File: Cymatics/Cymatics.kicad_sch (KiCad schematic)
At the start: 68 parts, among them IC1 LMV358IDR, IC2 MAX7403CSA+, IC3 LMV358IDR, IC4 LMV358IDR, IC5 MAX7403CSA+, J1 Screw_Terminal_01x03, J10 Screw_Terminal_01x04, J11 Screw_Terminal_01x05, J12 Screw_Terminal_01x02, J13 Screw_Terminal_01x02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

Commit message: resolved all DRC errors
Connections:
- net EXT_CS: now also J6.10 (Pin_10); no longer J6.15 (Pin_15)
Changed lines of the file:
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@@
-		)
-	)
-	(global_label "EXT_CS"
-		(shape output)
-		(at 147.32 226.06 180)
-		(fields_autoplaced yes)
-		(effects
-			(font
-				(size 1.27 1.27)
-			)
-			(justify right)
-		)
-		(property "Intersheetrefs" "${INTERSHEET_REFS}"
-			(at 137.5616 226.06 0)
-			(effects
-				(font
-					(size 1.27 1.27)
-				)
-				(justify right)
-				(hide yes)
-			)
 		)
 	)
@@
 				(hide yes)
 			)
+		)
+	)
+	(global_label "EXT_CS"
+		(shape output)
+		(at 147.32 213.36 180)
+		(fields_autoplaced yes)
+		(effects
+			(font
+				(size 1.27 1.27)
+			)
+			(justify right)
+		)
+		(property "Intersheetrefs" "${INTERSHEET_REFS}"
+			(at 137.5616 213.36 0)
+			(effects
+				(font
+					(size 1.27 1.27)
+				)
+				(justify right)
+				(hide yes)
+			)

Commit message: added testpoints
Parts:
- added TP1, TP2, TP3: TestPoint_2Pole, TestPoint:TestPoint_2Pads_Pitch2.54mm_Drill0.8mm, symbol Connector:TestPoint_2Pole
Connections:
- net GND: now also TP1.2, TP2.2, TP3.2
- net at IC1.7 (2OUT), IC2.2 (IN), R1.1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: now also TP1.1
- net at IC4.7 (2OUT), IC5.2 (IN), R2.2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: now also TP2.1
- net at R1.2, R2.1, U2.2 (IN): now also TP3.1
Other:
- moved on the sheet: C1, C10, C11, C12, C13, C14, C15, C16, C18, C19, C2, C3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

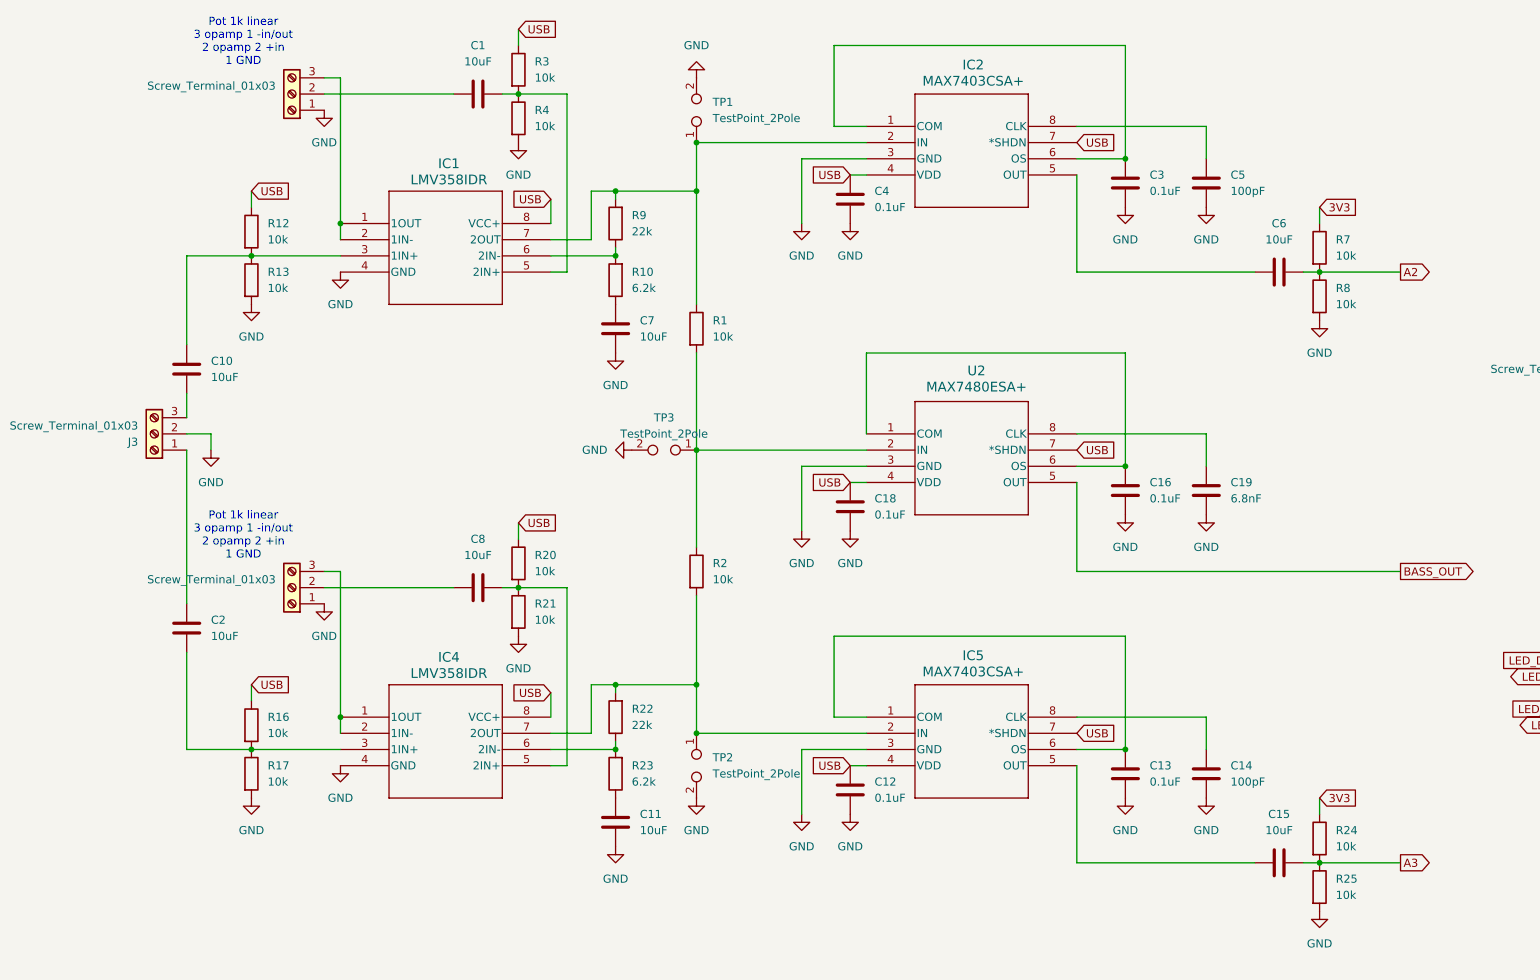
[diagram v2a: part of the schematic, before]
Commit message: testpoints update and terminal block labels
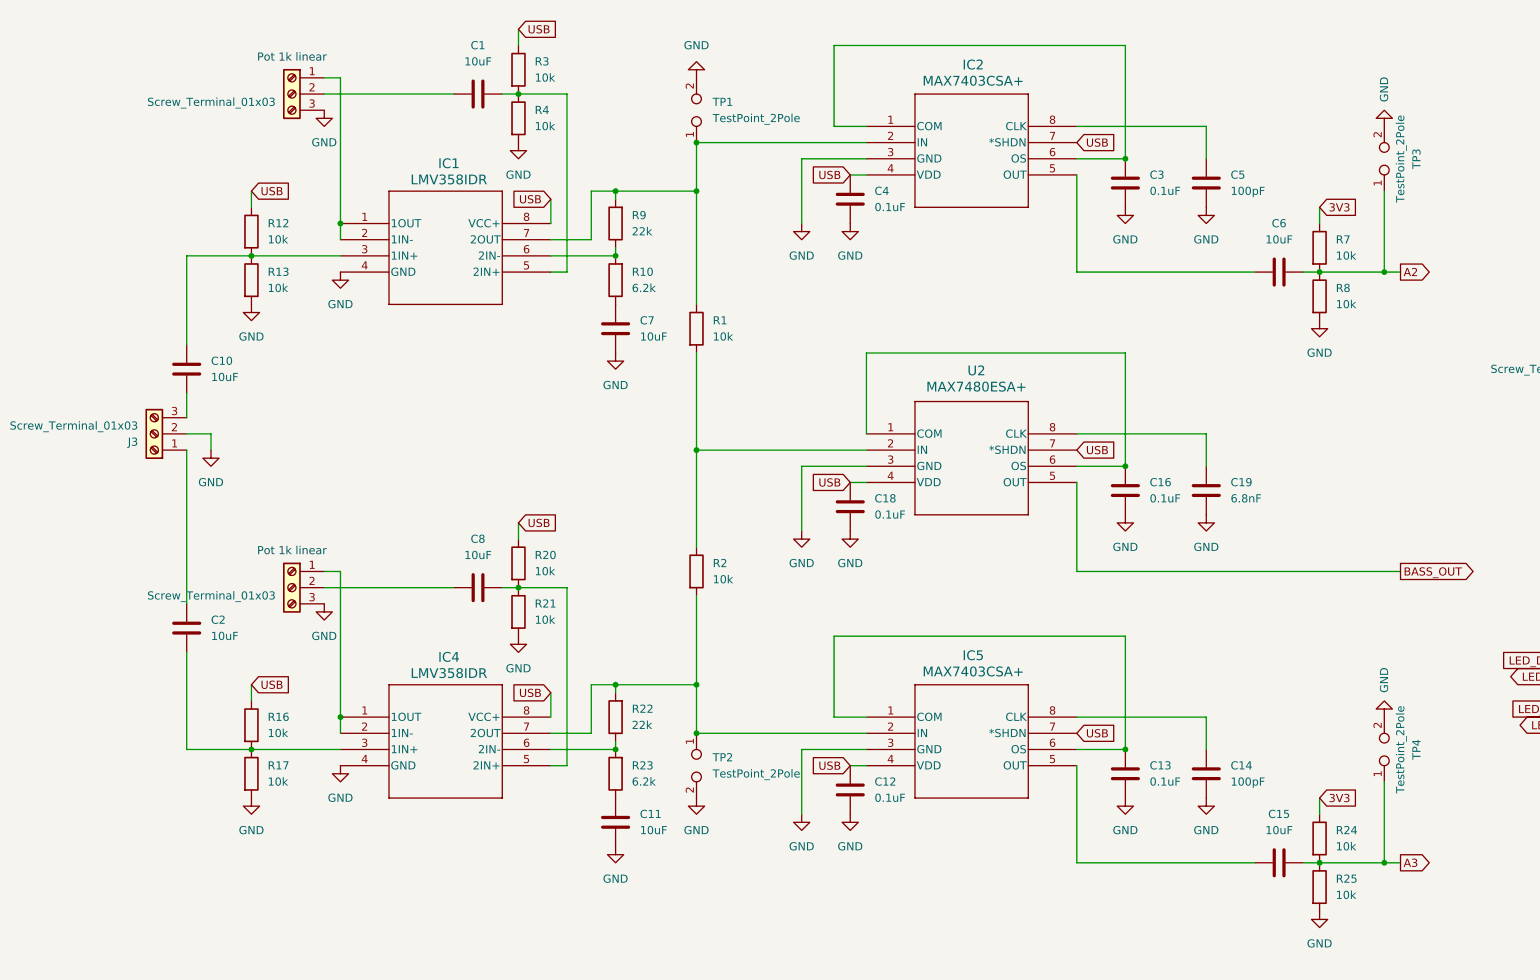
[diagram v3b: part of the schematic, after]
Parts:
- added TP4: TestPoint_2Pole, TestPoint:TestPoint_2Pads_Pitch2.54mm_Drill0.8mm, symbol Connector:TestPoint_2Pole
- C1, C10, C11, C15, C2, C6, C7, C8, J1, J16, J3, J4: In Stock 01-31-25 (none) -> 12
- C12, C13, C16, C18, C3, C4, C9: In Stock 01-31-25 (none) -> 10
- C14, C5, IC1, IC3, IC4, R10, R11, R14, R22, R23, R5, R6, R9: In Stock 01-31-25 (none) -> 8
- C17, IC2, IC5, J11, J6, J7, SD1, U1: In Stock 01-31-25 (none) -> 3
- C19, J18, TP1, TP2, TP3, U2: In Stock 01-31-25 (none) -> 0
- J10, J8: In Stock 01-31-25 (none) -> 4
- J12, J13, J15, J17, J2, J5, J9: In Stock 01-31-25 (none) -> 9
- R1, R12, R13, R16, R17, R18, R19, R2, R20, R21, R24, R25, R3, R4, R7, R8: In Stock 01-31-25 (none) -> 30
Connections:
- net A2: now also TP3.1
- net A3: now also TP4.1
- net GND: now also J16.3 (Pin_3), J4.3 (Pin_3), TP4.2; no longer J16.1 (Pin_1), J4.1 (Pin_1)
- net at IC1.1 (1OUT), IC1.2 (1IN-): now also J4.1 (Pin_1); no longer J4.3 (Pin_3)
- net at R1.2, R2.1, U2.2 (IN): no longer TP3.1
- net at IC4.1 (1OUT), IC4.2 (1IN-): now also J16.1 (Pin_1); no longer J16.3 (Pin_3)
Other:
- note added: "Pot 1k linear"
- note removed: "Pot 1k linear 3 opamp 1 -in/out 2 opamp 2 +in 1 GND"

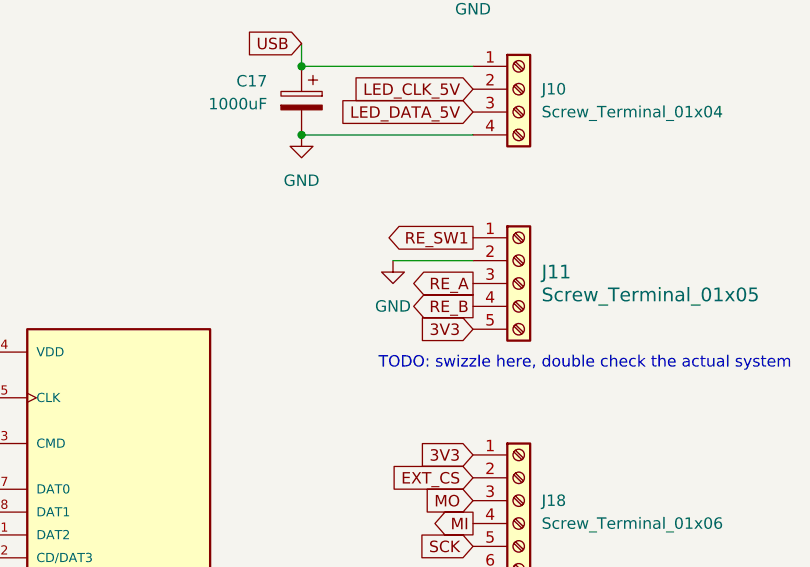
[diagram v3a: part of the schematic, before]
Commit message: swizzled rotary encoder block
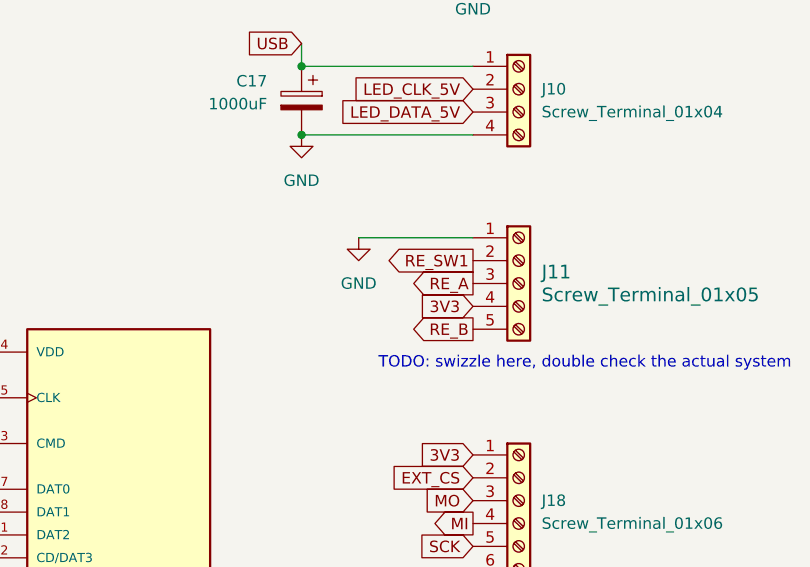
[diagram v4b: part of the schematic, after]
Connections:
- net 3V3: now also J11.4 (Pin_4); no longer J11.5 (Pin_5)
- net GND: now also J11.1 (Pin_1); no longer J11.2 (Pin_2)
- net RE_B: now also J11.5 (Pin_5); no longer J11.4 (Pin_4)
- net RE_SW1: now also J11.2 (Pin_2); no longer J11.1 (Pin_1)
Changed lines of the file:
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@@
 	(wire
 		(pts
-			(xy 358.14 177.8) (xy 367.03 177.8)
-		)
-		(stroke
-			(width 0)
-			(type default)
-		)
-	)
-	(wire
-		(pts
 			(xy 267.97 134.62) (xy 267.97 142.24)
 		)
@@
 	(wire
 		(pts
+			(xy 354.33 175.26) (xy 367.03 175.26)
+		)
+		(stroke
+			(width 0)
+			(type default)
+		)
+	)
+	(wire
+		(pts
 			(xy 321.31 76.2) (xy 321.31 83.82)
 		)
@@
 		)
 	)
-	(global_label "RE_B"
-		(shape output)
-		(at 367.03 182.88 180)
-		(fields_autoplaced yes)
-		(effects
-			(font
-				(size 1.27 1.27)
-			)
-			(justify right)
-		)
-		(property "Intersheetrefs" "${INTERSHEET_REFS}"
-			(at 359.3882 182.88 0)
-			(effects
-				(font
-					(size 1.27 1.27)
-				)
-				(justify right)
-				(hide yes)
-			)
-		)
-	)
 	(global_label "3V3"
 		(shape input)
@@
 		)
 	)
-	(global_label "3V3"
-		(shape input)
-		(at 367.03 185.42 180)
-		(fields_autoplaced yes)
-		(effects
-			(font
-				(size 1.27 1.27)
-			)
-			(justify right)
-		)
-		(property "Intersheetrefs" "${INTERSHEET_REFS}"
-			(at 360.5372 185.42 0)
-			(effects
-				(font
-					(size 1.27 1.27)
-				)
-				(justify right)
-				(hide yes)
-			)
-		)
-	)
 	(global_label "LED_CLK_3V3"
 		(shape input)
@@
 		)
 	)
-	(global_label "RE_SW1"
-		(shape output)
-		(at 367.03 175.26 180)
-		(fields_autoplaced yes)
-		(effects
-			(font
-				(size 1.27 1.27)
-			)
-			(justify right)
-		)
-		(property "Intersheetrefs" "${INTERSHEET_REFS}"
-			(at 356.7878 175.26 0)
-			(effects
-				(font
-					(size 1.27 1.27)
-				)
-				(justify right)
-				(hide yes)
-			)
-		)
-	)
 	(global_label "3V3"
 		(shape input)
@@
 		)
 	)
+	(global_label "RE_SW1"
+		(shape output)
+		(at 367.03 177.8 180)
+		(fields_autoplaced yes)
+		(effects
+			(font
+				(size 1.27 1.27)
+			)
+			(justify right)
+		)
+		(property "Intersheetrefs" "${INTERSHEET_REFS}"
+			(at 356.7878 177.8 0)
+			(effects
+				(font
+					(size 1.27 1.27)
+				)
+				(justify right)
+				(hide yes)
+			)
+		)
+	)
+	(global_label "RE_B"
+		(shape output)
+		(at 367.03 185.42 180)
+		(fields_autoplaced yes)
+		(effects
+			(font
+				(size 1.27 1.27)
+			)
+			(justify right)
+		)
+		(property "Intersheetrefs" "${INTERSHEET_REFS}"
+			(at 359.3882 185.42 0)
+			(effects
+				(font
+					(size 1.27 1.27)
+				)
+				(justify right)
+				(hide yes)
+			)
+		)
+	)
 	(global_label "USB"
 		(shape input)
@@
 		)
 	)
+	(global_label "3V3"
+		(shape input)
+		(at 367.03 182.88 180)
+		(fields_autoplaced yes)
+		(effects
+			(font
+				(size 1.27 1.27)
+			)
+			(justify right)
+		)
+		(property "Intersheetrefs" "${INTERSHEET_REFS}"
+			(at 360.5372 182.88 0)
+			(effects
+				(font
+					(size 1.27 1.27)
+				)
+				(justify right)
+				(hide yes)
+			)
+		)
+	)
 	(symbol
 		(lib_id "Device:R")
@@
 	(symbol
 		(lib_id "power:GND")
-		(at 358.14 177.8 0)
-		(unit 1)
-		(exclude_from_sim no)
-		(in_bom yes)
-		(on_board yes)
-		(dnp no)
-		(fields_autoplaced yes)
-		(property "Reference" "#PWR021"
-			(at 358.14 184.15 0)
-			(effects
-				(font
-					(size 1.27 1.27)
-				)
-				(hide yes)
-			)
-		)
-		(property "Value" "GND"
-			(at 358.14 182.88 0)
-			(effects
-				(font
-					(size 1.27 1.27)
-				)
-			)
-		)
-		(property "Footprint" ""
-			(at 358.14 177.8 0)
-			(effects
-				(font
-					(size 1.27 1.27)
-				)
-				(hide yes)
-			)
-		)
-		(property "Datasheet" ""
-			(at 358.14 177.8 0)
-			(effects
-				(font
-					(size 1.27 1.27)
-				)
-				(hide yes)
-			)
-		)
-		(property "Description" "Power symbol creates a global label with name \"GND\" , ground"
-			(at 358.14 177.8 0)
-			(effects
-				(font
-					(size 1.27 1.27)
-				)
-				(hide yes)
-			)
-		)
-		(pin "1"
-		)
-		(instances
-			(project "AudioLux"
-				(path "/c40baf00-5d70-4382-8f24-d28e6ebf545d"
-					(reference "#PWR021")
-					(unit 1)
-				)
-			)
-		)
-	)
-	(symbol
-		(lib_id "power:GND")
 		(at 139.7 153.67 0)
 		(unit 1)
@@
 					(unit 1)
 				)
+			)
+		)
+	)
+	(symbol
+		(lib_id "power:GND")
+		(at 354.33 175.26 0)
+		(unit 1)
+		(exclude_from_sim no)
+		(in_bom yes)
+		(on_board yes)
+		(dnp no)
+		(fields_autoplaced yes)
+		(property "Reference" "#PWR021"
+			(at 354.33 181.61 0)
+			(effects
+				(font
+					(size 1.27 1.27)
+				)
+				(hide yes)
+			)
+		)
+		(property "Value" "GND"
+			(at 354.33 180.34 0)
+			(effects
+				(font
+					(size 1.27 1.27)
+				)
+			)
+		)
+		(property "Footprint" ""
+			(at 354.33 175.26 0)
+			(effects
+				(font
+					(size 1.27 1.27)
+				)
+				(hide yes)
+			)
+		)
+		(property "Datasheet" ""
+			(at 354.33 175.26 0)
+			(effects
+				(font
+					(size 1.27 1.27)
+				)
+				(hide yes)
+			)
+		)
+		(property "Description" "Power symbol creates a global label with name \"GND\" , ground"
+			(at 354.33 175.26 0)
+			(effects
+				(font
+					(size 1.27 1.27)
+				)
+				(hide yes)
+			)
+		)
+		(pin "1"
+		)
+		(instances
+			(project "Cymatics"
+				(path "/c40baf00-5d70-4382-8f24-d28e6ebf545d"
+					(reference "#PWR021")
+					(unit 1)
+				)

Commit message: new testpoint RCU-0C
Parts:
- removed TP1, TP2, TP3, TP4: TestPoint_2Pole, TestPoint:TestPoint_2Pads_Pitch2.54mm_Drill0.8mm, symbol Connector:TestPoint_2Pole
- added J14, J19, J20, J21, J22, J23, J24: RCU-0C, CONN1_RCU-0C_TEC, symbol RCU-0C:RCU-0C
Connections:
- net A2: now also J22.1
- net A3: now also J23.1
- net GND: now also J19.1, J21.1, J24.1
- net at IC1.7 (2OUT), IC2.2 (IN), R1.1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: now also J14.1
- net at IC4.7 (2OUT), IC5.2 (IN), R2.2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: now also J20.1

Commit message: changes and Gerber Drill generate for order
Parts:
- C1, C10, C11, C15, C2, C6, C7, C8: In Stock 02-01-25 (none) -> 8; To Order 02-01-25 (none) -> 10
- C12, C13, C16, C18, C3, C4, C9: In Stock 02-01-25 (none) -> 5; To Order 02-01-25 (none) -> 10
- C14, C5, R10, R11, R14, R22, R23, R5, R6, R9: In Stock 02-01-25 (none) -> 7; To Order 02-01-25 (none) -> 0
- C17, IC2, IC5, J11, J6, J7, SD1, U1: In Stock 02-01-25 (none) -> 2; To Order 02-01-25 (none) -> 0
- C19: In Stock 02-01-25 (none) -> 0; To Order 02-01-25 (none) -> 10
- IC1, IC3, IC4, J12, J13, J15, J17, J2, J5, J9: In Stock 02-01-25 (none) -> 6; To Order 02-01-25 (none) -> 0
- J1, J16, J3, J4: In Stock 02-01-25 (none) -> 10; To Order 02-01-25 (none) -> 0
- J10, J8: In Stock 02-01-25 (none) -> 3; To Order 02-01-25 (none) -> 0
- J14, J19, J20, J21, J22, J23, J24: In Stock 01-31-25 (none) -> 0; In Stock 02-01-25 (none) -> 0; To Order 02-01-25 (none) -> 10
- J18: In Stock 02-01-25 (none) -> 0; To Order 02-01-25 (none) -> 0
- R1, R12, R13, R16, R17, R18, R19, R2, R20, R21, R24, R25, R3, R4, R7, R8: In Stock 02-01-25 (none) -> 20; To Order 02-01-25 (none) -> 0
- U2: In Stock 02-01-25 (none) -> 0; To Order 02-01-25 (none) -> 1

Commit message: changed positioning of blocks for diagrams
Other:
- note removed: "TODO: just use 3V3?"
- note removed: "TODO: swizzle here, double check the actual system"
- moved on the sheet: C1, C10, C11, C12, C13, C14, C15, C16, C17, C18, C19, C2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

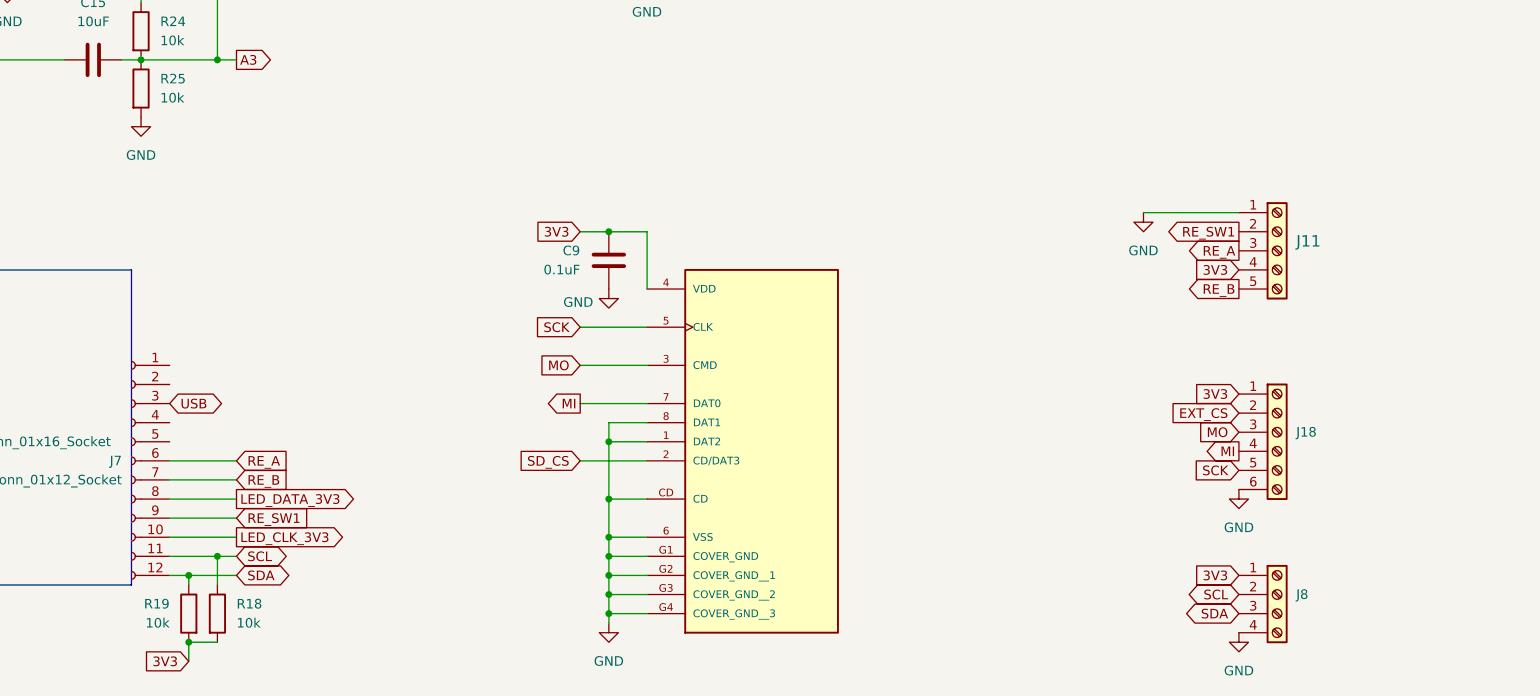
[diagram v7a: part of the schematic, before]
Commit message: pull up resistors for SPI and I2C
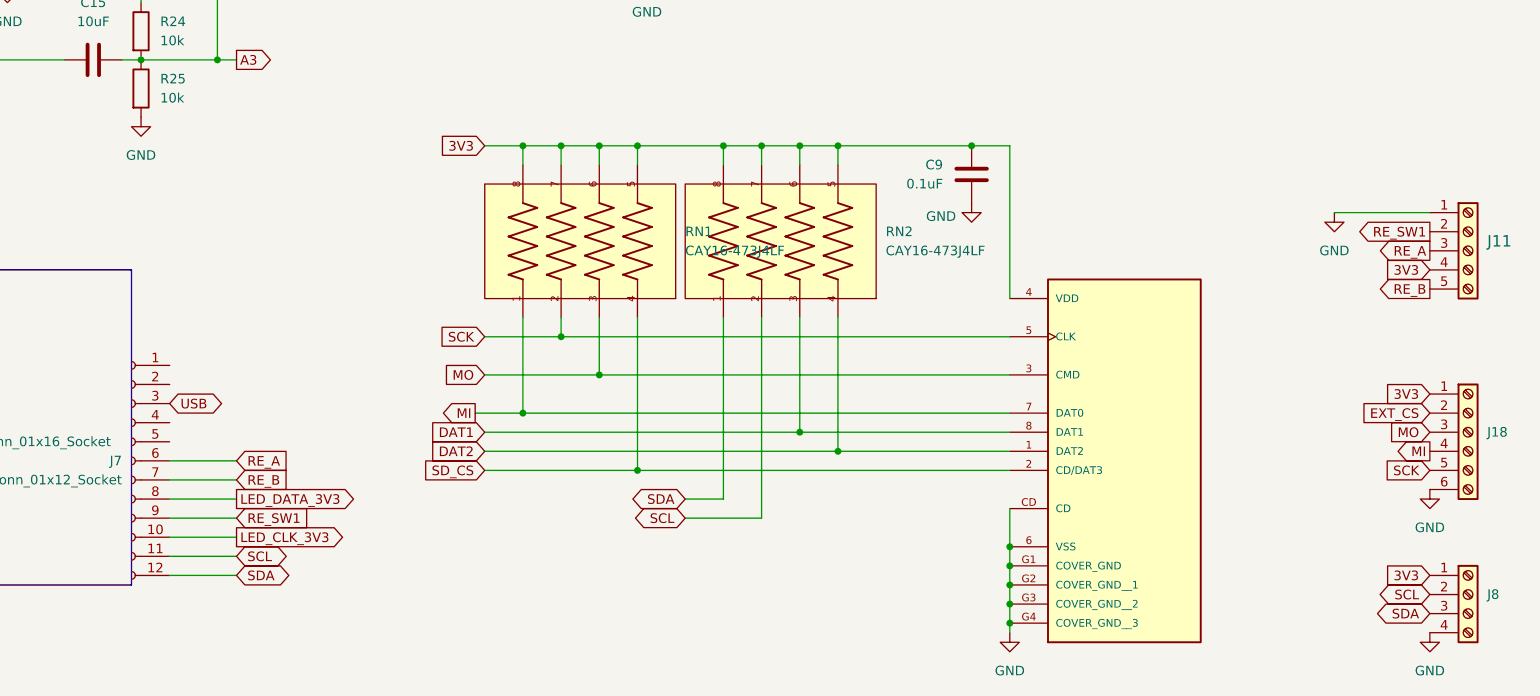
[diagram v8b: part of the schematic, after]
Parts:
- removed R18, R19: 10k, Resistor_SMD:R_1206_3216Metric, symbol Device:R
- added RN1, RN2: CAY16-473J4LF, CAY16:RESCAF80P320X160X60-8N, symbol CAY16:CAY16-473J4LF
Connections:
- net 3V3: now also RN1.5, RN1.6, RN1.7, RN1.8, RN2.5, RN2.6, RN2.7, RN2.8
- net GND: no longer SD1.1 (DAT2), SD1.8 (DAT1)
- net MI: now also RN1.1
- net MO: now also RN1.3
- net SCK: now also RN1.2
- net SCL: now also RN2.2
- net SDA: now also RN2.1
- net SD_CS: now also RN1.4
- new net DAT1: RN2.3, SD1.8 (DAT1)
- new net DAT2: RN2.4, SD1.1 (DAT2)
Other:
- moved on the sheet: C9, J11, J18, J8
